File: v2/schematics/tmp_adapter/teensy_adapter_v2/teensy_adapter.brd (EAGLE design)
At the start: 66.8 x 67 mm, 70 parts, among them IC1 TEENSY 3.6, IC2 ATMEGA1284P, IC3 MAX803REXR, IC4 DRV8835, IC5 L293D, J1 RADL, J10 RADL, J11 RADR, J12 Erw_PWM_1, J13 SWD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

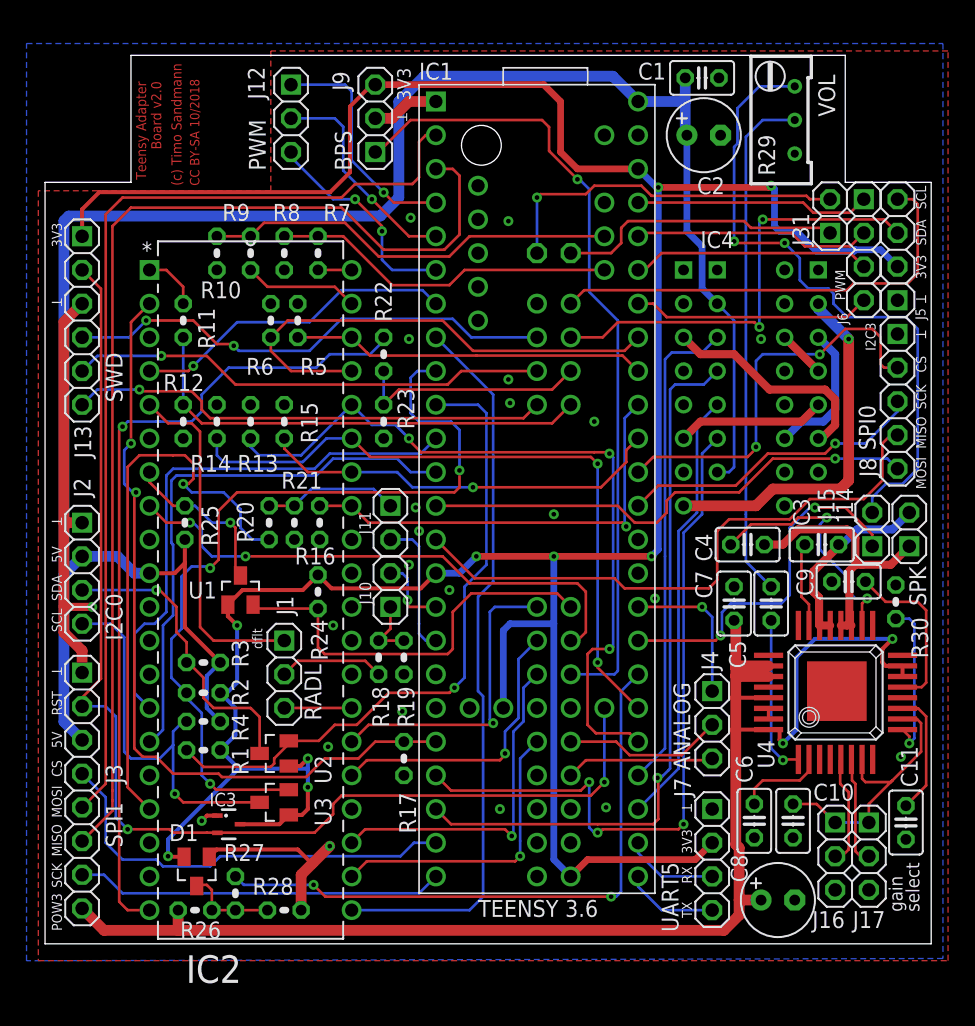
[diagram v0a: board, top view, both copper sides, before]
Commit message: teensy adapter board v2 updated: bugfix silkscreen
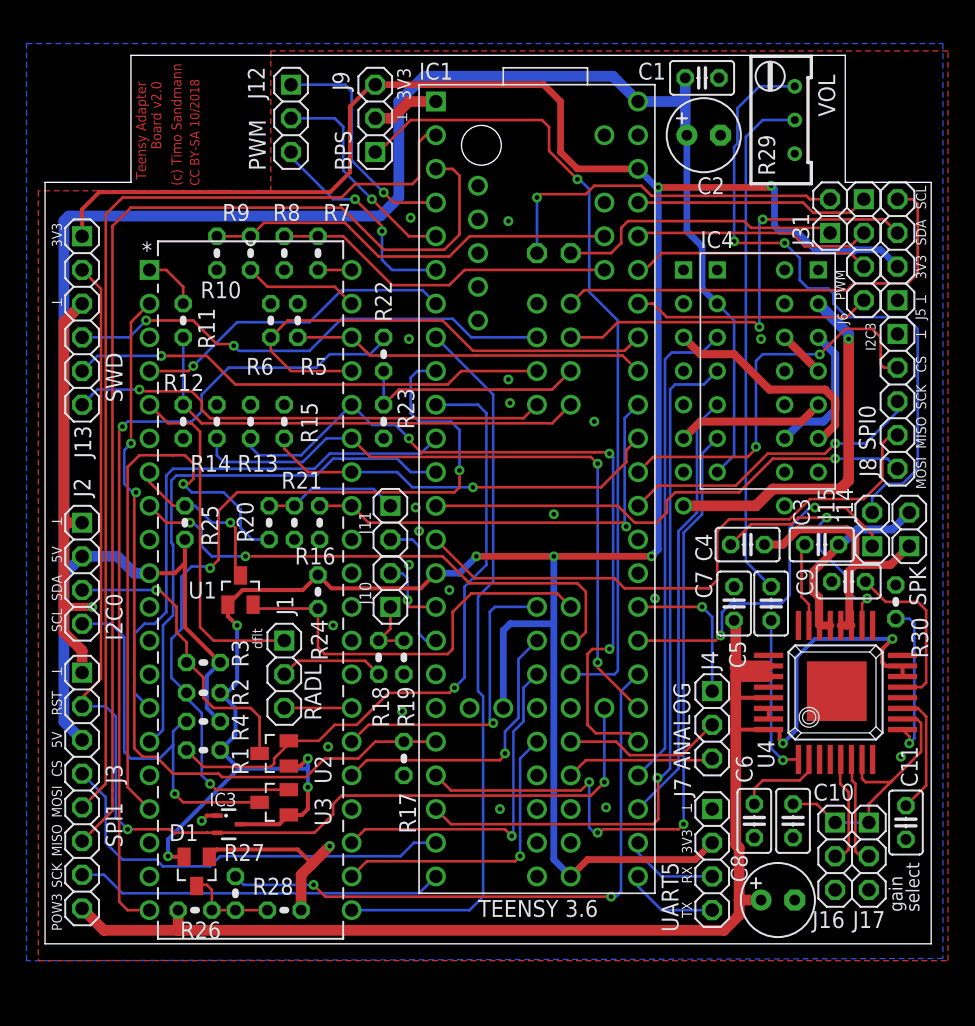
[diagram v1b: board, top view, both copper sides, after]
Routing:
- net +5V: track 154.6 -> 154.1 mm

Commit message: bugfix teensy adapter schematic: teensy pin 49/50 naming updated
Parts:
- C10: value 10n -> 10nF
- C11, C5, C6, C7, C9: value 1u -> 1uF
- C3, C4: value 220n -> 220nF
- C8: value 220u -> 220uF
- J1: value RADL -> RADL_SEL
- R29: value 5K -> 5k
- R30: value 100K -> 100k
- moved J32 1.27 mm to (38.4, 54.6)
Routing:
- net BPS_3V3: track 61.2 -> 63.6 mm
- net KL02_DD: track 27.1 -> 28.3 mm
- net ABSTL_3V3: track 26.1 -> 27.2 mm
- net KL02_DC: track 21.6 -> 22.5 mm
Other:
- board text added: "CC BY-SA 11/2018"
- board text added: "Teensy Adapter Board v2.1"
- board text removed: "CC BY-SA 10/2018"
- board text removed: "Teensy Adapter Board v2.0"
